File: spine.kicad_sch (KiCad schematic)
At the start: 0 parts

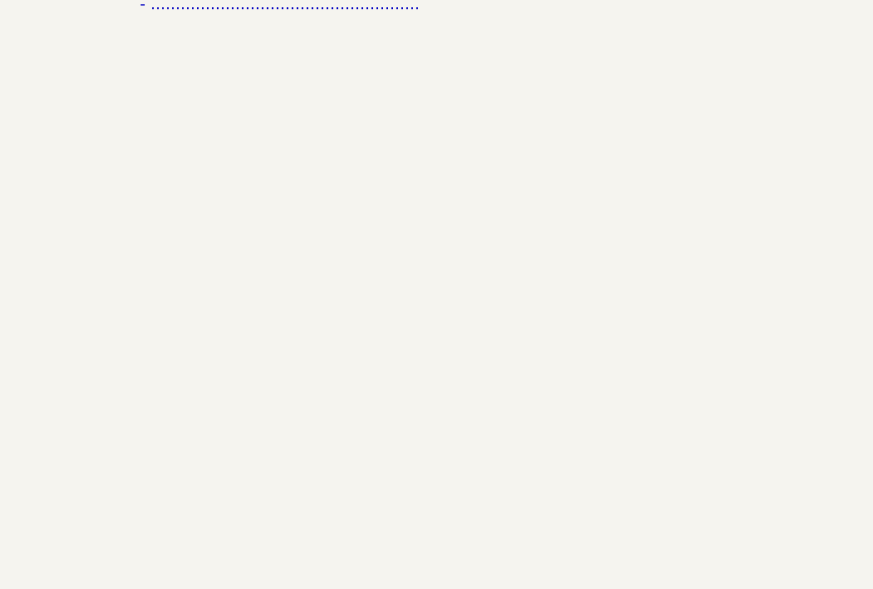
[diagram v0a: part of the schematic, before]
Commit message: add: connectors
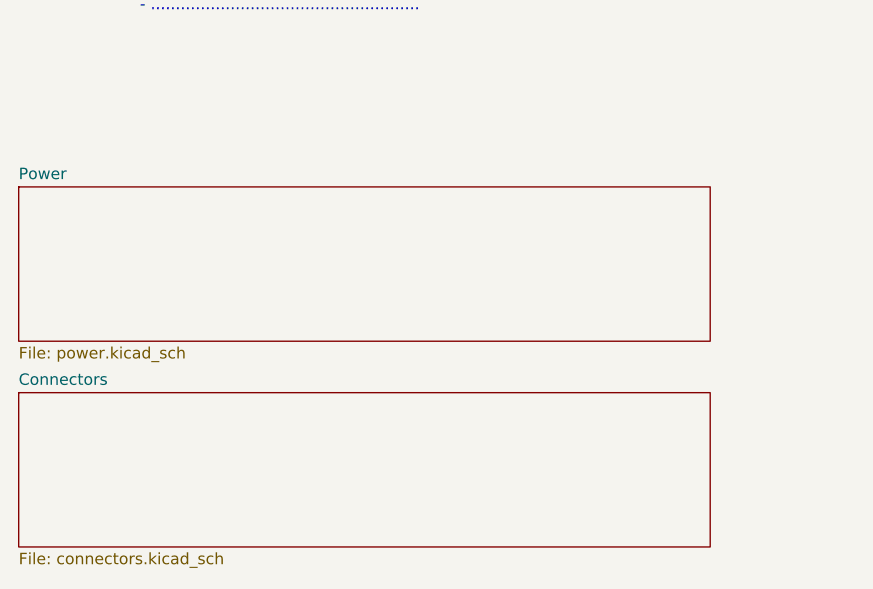
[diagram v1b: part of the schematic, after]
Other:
- added sheet Connectors (connectors.kicad_sch)
- added sheet Power (power.kicad_sch)
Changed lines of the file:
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@@
+		)
+	)
+	(sheet
+		(at 10.16 213.36)
+		(size 76.835 17.145)
+		(exclude_from_sim no)
+		(in_bom yes)
+		(on_board yes)
+		(dnp no)
+		(fields_autoplaced yes)
+		(stroke
+			(width 0.1524)
+			(type solid)
+		)
+		(fill
+			(color 0 0 0 0.0000)
+		)
+		(property "Sheetname" "Power"
+			(at 10.16 212.6484 0)
+			(effects
+				(font
+					(size 1.27 1.27)
+				)
+				(justify left bottom)
+			)
+		)
+		(property "Sheetfile" "power.kicad_sch"
+			(at 10.16 231.0896 0)
+			(effects
+				(font
+					(size 1.27 1.27)
+				)
+				(justify left top)
+			)
+		)
+		(instances
+			(project "spine"
+				(path "/9b29516b-1745-41d0-bc5f-f6cf48cfb4af"
+					(page "2")
+				)
+			)
+		)
+	)
+	(sheet
+		(at 10.16 236.22)
+		(size 76.835 17.145)
+		(exclude_from_sim no)
+		(in_bom yes)
+		(on_board yes)
+		(dnp no)
+		(fields_autoplaced yes)
+		(stroke
+			(width 0.1524)
+			(type solid)
+		)
+		(fill
+			(color 0 0 0 0.0000)
+		)
+		(property "Sheetname" "Connectors"
+			(at 10.16 235.5084 0)
+			(effects
+				(font
+					(size 1.27 1.27)
+				)
+				(justify left bottom)
+			)
+		)
+		(property "Sheetfile" "connectors.kicad_sch"
+			(at 10.16 253.9496 0)
+			(effects
+				(font
+					(size 1.27 1.27)
+				)
+				(justify left top)
+			)
+		)
+		(instances
+			(project "spine"
+				(path "/9b29516b-1745-41d0-bc5f-f6cf48cfb4af"
+					(page "3")
+				)
+			)
 		)
 	)
